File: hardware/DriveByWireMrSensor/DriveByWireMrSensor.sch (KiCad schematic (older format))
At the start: 5 parts, among them J1 Conn_01x03_Female, U1 LM358, U2 KMZ49_118

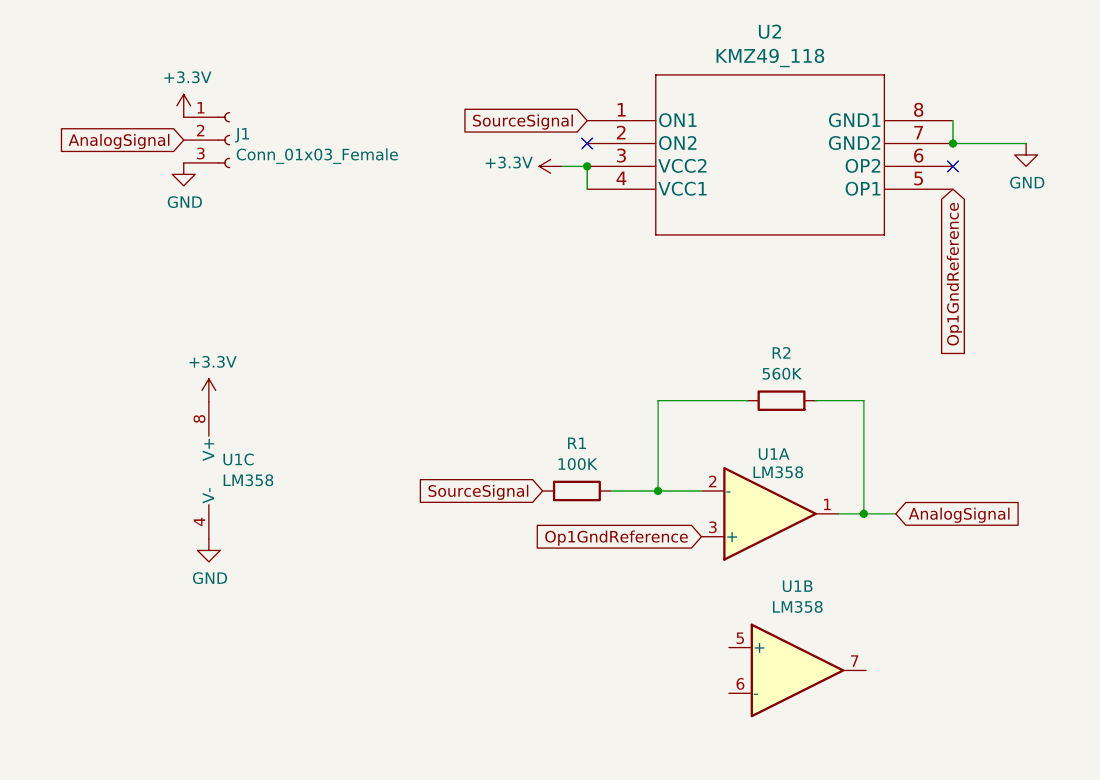
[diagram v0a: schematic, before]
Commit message: adding second opamp into circuit
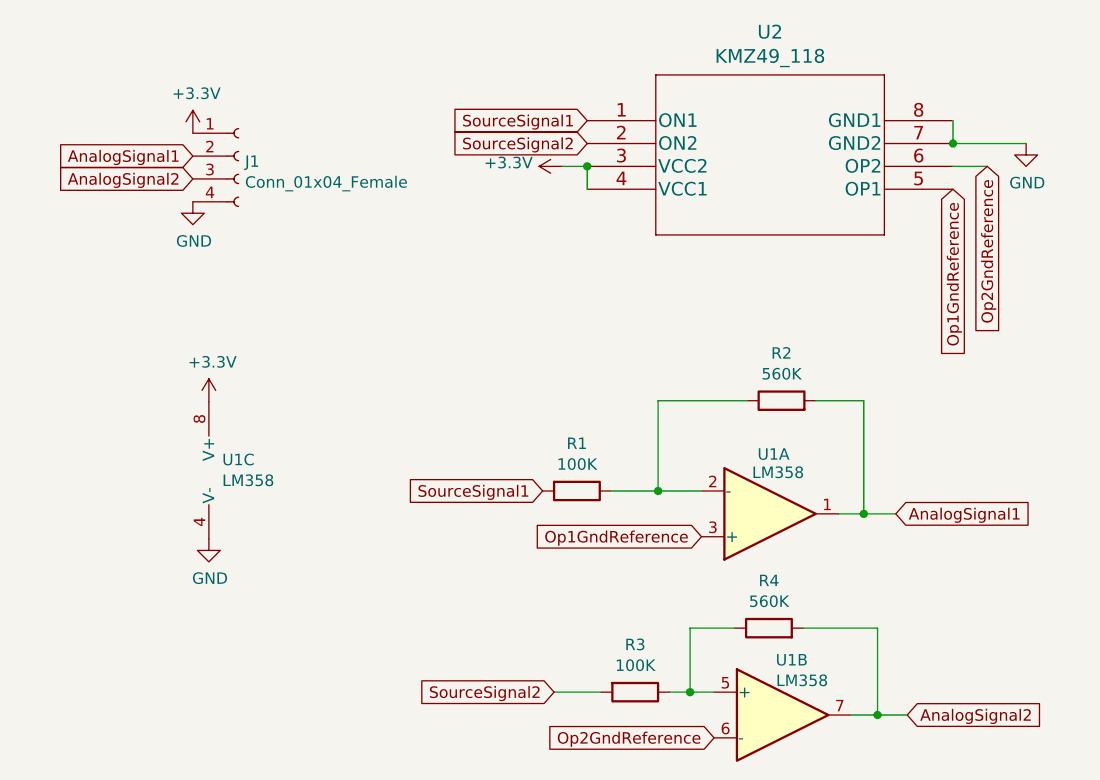
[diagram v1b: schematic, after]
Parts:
- removed J1: Conn_01x03_Female, Connector_PinHeader_2.54mm:PinHeader_1x03_P2.54mm_Vertical, symbol Connector:Conn_01x03_Female
- added J1: Conn_01x04_Female, symbol Connector:Conn_01x04_Female
- added R3: 100K, Resistor_SMD:R_0805_2012Metric_Pad1.15x1.40mm_HandSolder, symbol Device:R
- added R4: 560K, Resistor_SMD:R_0805_2012Metric_Pad1.15x1.40mm_HandSolder, symbol Device:R
- U1: footprint (none) -> UsefulModifications:LM358PSR
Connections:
- net +3V3: now also J1.1 (Pin_1)
- net GND: now also J1.4 (Pin_4)
- net SourceSignal2: now reaches U2.2 (ON2)
- net SourceSignal2: now also R3.2
- net Op2GndReference: now reaches U2.6 (OP2)
- net Op2GndReference: now also U1.6 (-)
- net at U1.5 (+): now also R3.1, R4.1
- net AnalogSignal2: now reaches U1.7
- net AnalogSignal2: now also J1.3 (Pin_3), R4.2
- net AnalogSignal renamed AnalogSignal1
- net AnalogSignal1: now also J1.2 (Pin_2)
- net SourceSignal renamed SourceSignal1
- no-connect marks 2 -> 0
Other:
- moved on the sheet: U1B
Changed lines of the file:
@@
-$EndComp
-$Comp
-L Connector:Conn_01x03_Female J1
-U 1 1 6189EBE1
-P 3630 2545
-F 0 "J1" H 3658 2571 50  0000 L CNN
-F 1 "Conn_01x03_Female" H 3658 2480 50  0000 L CNN
-F 2 "Connector_PinHeader_2.54mm:PinHeader_1x03_P2.54mm_Vertical" H 3630 2545 50  0001 C CNN
-F 3 "~" H 3630 2545 50  0001 C CNN
-	1    3630 2545
-	1    0    0    -1
 $EndComp
 $Comp
 L power:+3.3V #PWR0101
 U 1 1 6189F625
-P 3430 2445
-F 0 "#PWR0101" H 3430 2295 50  0001 C CNN
-F 1 "+3.3V" H 3445 2618 50  0000 C CNN
-F 2 "" H 3430 2445 50  0001 C CNN
-F 3 "" H 3430 2445 50  0001 C CNN
-	1    3430 2445
+P 3470 2515
+F 0 "#PWR0101" H 3470 2365 50  0001 C CNN
+F 1 "+3.3V" H 3485 2688 50  0000 C CNN
+F 2 "" H 3470 2515 50  0001 C CNN
+F 3 "" H 3470 2515 50  0001 C CNN
+	1    3470 2515
 	1    0    0    -1
 $EndComp
@@
 L power:GND #PWR0102
 U 1 1 618A05B7
-P 3430 2645
-F 0 "#PWR0102" H 3430 2395 50  0001 C CNN
-F 1 "GND" H 3435 2472 50  0000 C CNN
-F 2 "" H 3430 2645 50  0001 C CNN
-F 3 "" H 3430 2645 50  0001 C CNN
-	1    3430 2645
-	1    0    0    -1
-$EndComp
-Text GLabel 3430 2545 0    50   Input ~ 0
-AnalogSignal
+P 3470 2815
+F 0 "#PWR0102" H 3470 2565 50  0001 C CNN
+F 1 "GND" H 3475 2642 50  0000 C CNN
+F 2 "" H 3470 2815 50  0001 C CNN
+F 3 "" H 3470 2815 50  0001 C CNN
+	1    3470 2815
+	1    0    0    -1
+$EndComp
+Text GLabel 3470 2615 0    50   Input ~ 0
+AnalogSignal1
 $Comp
 L power:+3.3V #PWR0103
@@
 $EndComp
 Text GLabel 6545 4180 2    50   Input ~ 0
-AnalogSignal
+AnalogSignal1
 Text GLabel 6795 2760 3    50   Input ~ 0
 Op1GndReference
 Text GLabel 5695 4280 0    50   Input ~ 0
 Op1GndReference
-NoConn ~ 6795 2660
-NoConn ~ 5195 2560
 Text GLabel 5195 2460 0    50   Input ~ 0
-SourceSignal
+SourceSignal1
 Text GLabel 5000 4080 0    50   Input ~ 0
-SourceSignal
+SourceSignal1
 $Comp
 L Amplifier_Operational:LM358 U1
@@
 L Amplifier_Operational:LM358 U1
 U 2 1 618E9970
-P 6115 4865
-F 0 "U1" H 6115 5232 50  0000 C CNN
-F 1 "LM358" H 6115 5141 50  0000 C CNN
-F 2 "" H 6115 4865 50  0001 C CNN
-F 3 "http://www.ti.com/lit/ds/symlink/lm2904-n.pdf" H 6115 4865 50  0001 C CNN
-	2    6115 4865
-	1    0    0    -1
-$EndComp
+P 6050 5060
+F 0 "U1" H 6090 5300 50  0000 C CNN
+F 1 "LM358" H 6135 5210 50  0000 C CNN
+F 2 "UsefulModifications:LM358PSR" H 6050 5060 50  0001 C CNN
+F 3 "http://www.ti.com/lit/ds/symlink/lm2904-n.pdf" H 6050 5060 50  0001 C CNN
+	2    6050 5060
+	1    0    0    -1
+$EndComp
+$Comp
+L Device:R R4
+U 1 1 618DED44
+P 5990 4680
+F 0 "R4" V 6197 4680 50  0000 C CNN
+F 1 "560K" V 6106 4680 50  0000 C CNN
+F 2 "Resistor_SMD:R_0805_2012Metric_Pad1.15x1.40mm_HandSolder" V 5920 4680 50  0001 C CNN
+F 3 "~" H 5990 4680 50  0001 C CNN
+	1    5990 4680
+	0    -1   -1   0
+$EndComp
+$Comp
+L Device:R R3
+U 1 1 618E050D
+P 5405 4960
+F 0 "R3" V 5198 4960 50  0000 C CNN
+F 1 "100K" V 5289 4960 50  0000 C CNN
+F 2 "Resistor_SMD:R_0805_2012Metric_Pad1.15x1.40mm_HandSolder" V 5335 4960 50  0001 C CNN
+F 3 "~" H 5405 4960 50  0001 C CNN
+	1    5405 4960
+	0    1    1    0
+$EndComp
+$Comp
+L Connector:Conn_01x04_Female J1
+U 1 1 618E11C5
+P 3670 2615
+F 0 "J1" H 3698 2591 50  0000 L CNN
+F 1 "Conn_01x04_Female" H 3698 2500 50  0000 L CNN
+F 2 "" H 3670 2615 50  0001 C CNN
+F 3 "~" H 3670 2615 50  0001 C CNN
+	1    3670 2615
+	1    0    0    -1
+$EndComp
+Text GLabel 3470 2715 0    50   Input ~ 0
+AnalogSignal2
+Text GLabel 6945 2660 3    50   Input ~ 0
+Op2GndReference
+Wire Wire Line
+	6795 2660 6945 2660
+Text GLabel 5195 2560 0    50   Input ~ 0
+SourceSignal2
+Text GLabel 5050 4960 0    50   Input ~ 0
+SourceSignal2
+Text GLabel 5750 5160 0    50   Input ~ 0
+Op2GndReference
+Text GLabel 6595 5060 2    50   Input ~ 0
+AnalogSignal2
+Wire Wire Line
+	6350 5060 6465 5060
+Wire Wire Line
+	6140 4680 6465 4680
+Wire Wire Line
+	6465 4680 6465 5060
+Connection ~ 6465 5060
+Wire Wire Line
+	6465 5060 6595 5060
+Wire Wire Line
+	5555 4960 5645 4960
+Wire Wire Line
+	5840 4680 5645 4680
+Wire Wire Line
+	5645 4680 5645 4960
+Connection ~ 5645 4960
+Wire Wire Line
+	5645 4960 5750 4960
+Wire Wire Line
+	5050 4960 5255 4960
 $EndSCHEMATC

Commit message: drive by wire pcb
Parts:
- J1: footprint (none) -> Connector_PinHeader_2.54mm:PinHeader_1x04_P2.54mm_Vertical
- R1, R3: value 100K -> 10K
- R2, R4: value 560K -> 100K
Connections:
- net Op2GndReference: now also U1.5 (+); no longer U1.6 (-)
- net at R3.1, R4.1: now also U1.6 (-); no longer U1.5 (+)
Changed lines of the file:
@@
 P 5150 4080
 F 0 "R1" V 4943 4080 50  0000 C CNN
-F 1 "100K" V 5034 4080 50  0000 C CNN
+F 1 "10K" V 5034 4080 50  0000 C CNN
 F 2 "Resistor_SMD:R_0805_2012Metric_Pad1.15x1.40mm_HandSolder" V 5080 4080 50  0001 C CNN
 F 3 "~" H 5150 4080 50  0001 C CNN
@@
 P 6045 3685
 F 0 "R2" V 6252 3685 50  0000 C CNN
-F 1 "560K" V 6161 3685 50  0000 C CNN
+F 1 "100K" V 6161 3685 50  0000 C CNN
 F 2 "Resistor_SMD:R_0805_2012Metric_Pad1.15x1.40mm_HandSolder" V 5975 3685 50  0001 C CNN
 F 3 "~" H 6045 3685 50  0001 C CNN
@@
 F 3 "http://www.ti.com/lit/ds/symlink/lm2904-n.pdf" H 6050 5060 50  0001 C CNN
 	2    6050 5060
-	1    0    0    -1
+	1    0    0    1
 $EndComp
 $Comp
@@
 P 5990 4680
 F 0 "R4" V 6197 4680 50  0000 C CNN
-F 1 "560K" V 6106 4680 50  0000 C CNN
+F 1 "100K" V 6106 4680 50  0000 C CNN
 F 2 "Resistor_SMD:R_0805_2012Metric_Pad1.15x1.40mm_HandSolder" V 5920 4680 50  0001 C CNN
 F 3 "~" H 5990 4680 50  0001 C CNN
@@
 P 5405 4960
 F 0 "R3" V 5198 4960 50  0000 C CNN
-F 1 "100K" V 5289 4960 50  0000 C CNN
+F 1 "10K" V 5289 4960 50  0000 C CNN
 F 2 "Resistor_SMD:R_0805_2012Metric_Pad1.15x1.40mm_HandSolder" V 5335 4960 50  0001 C CNN
 F 3 "~" H 5405 4960 50  0001 C CNN
@@
 F 0 "J1" H 3698 2591 50  0000 L CNN
 F 1 "Conn_01x04_Female" H 3698 2500 50  0000 L CNN
-F 2 "" H 3670 2615 50  0001 C CNN
+F 2 "Connector_PinHeader_2.54mm:PinHeader_1x04_P2.54mm_Vertical" H 3670 2615 50  0001 C CNN
 F 3 "~" H 3670 2615 50  0001 C CNN
 	1    3670 2615
